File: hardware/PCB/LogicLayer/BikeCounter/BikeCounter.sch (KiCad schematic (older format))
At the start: 18 parts, among them J1 PIR sensor connector (TWIG-4P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, J2 Conn_01x04_Female, J3 Conn_01x02_Female, SW1 SW_DIP_x03, U1 DS3231M

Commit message: PCB layout splitted into power and logic layer
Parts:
- removed BT1: Battery_Cell, Battery:BatteryHolder_Keystone_1042_1x18650, symbol Device:Battery_Cell
- removed J3: Conn_01x02_Female, symbol Connector:Conn_01x02_Female
- added J3: Vbat, Connector_PinSocket_2.54mm:PinSocket_1x01_P2.54mm_Vertical, symbol Connector:Conn_01x01_Female
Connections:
- net labels removed: +3V8
- wire segments 72 -> 65
- no-connect marks 26 -> 27
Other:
- moved on the sheet: C1, J1, R1, R2
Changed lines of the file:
@@
-$EndComp
-$Comp
-L Device:Battery_Cell BT1
-U 1 1 615B5A8C
-P 3300 1950
-F 0 "BT1" H 3418 2046 50  0000 L CNN
-F 1 "Battery_Cell" H 3418 1955 50  0000 L CNN
-F 2 "Battery:BatteryHolder_Keystone_1042_1x18650" V 3300 2010 50  0001 C CNN
-F 3 "~" V 3300 2010 50  0001 C CNN
-	1    3300 1950
-	1    0    0    -1
-$EndComp
-$Comp
-L power:+3V8 #PWR0101
-U 1 1 615B6BD8
-P 3300 1750
-F 0 "#PWR0101" H 3300 1600 50  0001 C CNN
-F 1 "+3V8" H 3315 1923 50  0000 C CNN
-F 2 "" H 3300 1750 50  0001 C CNN
-F 3 "" H 3300 1750 50  0001 C CNN
-	1    3300 1750
-	1    0    0    -1
-$EndComp
-$Comp
-L power:+3V8 #PWR0102
-U 1 1 615B7800
-P 4350 2100
-F 0 "#PWR0102" H 4350 1950 50  0001 C CNN
-F 1 "+3V8" H 4365 2273 50  0000 C CNN
-F 2 "" H 4350 2100 50  0001 C CNN
-F 3 "" H 4350 2100 50  0001 C CNN
-	1    4350 2100
-	1    0    0    -1
-$EndComp
-$Comp
-L power:GND #PWR0103
-U 1 1 615B8DA8
-P 3300 2050
-F 0 "#PWR0103" H 3300 1800 50  0001 C CNN
-F 1 "GND" H 3305 1877 50  0000 C CNN
-F 2 "" H 3300 2050 50  0001 C CNN
-F 3 "" H 3300 2050 50  0001 C CNN
-	1    3300 2050
-	1    0    0    -1
 $EndComp
 $Comp
 L Device:R R2
 U 1 1 615B9C8E
-P 4050 2750
-F 0 "R2" H 4120 2796 50  0000 L CNN
-F 1 "1.2M" H 4120 2705 50  0000 L CNN
-F 2 "Resistor_SMD:R_1206_3216Metric_Pad1.42x1.75mm_HandSolder" V 3980 2750 50  0001 C CNN
-F 3 "~" H 4050 2750 50  0001 C CNN
-	1    4050 2750
+P 4050 3700
+F 0 "R2" H 4120 3746 50  0000 L CNN
+F 1 "1.2M" H 4120 3655 50  0000 L CNN
+F 2 "Resistor_SMD:R_1206_3216Metric_Pad1.42x1.75mm_HandSolder" V 3980 3700 50  0001 C CNN
+F 3 "~" H 4050 3700 50  0001 C CNN
+	1    4050 3700
 	1    0    0    -1
 $EndComp
@@
 L Device:R R1
 U 1 1 615BA347
-P 4050 2350
-F 0 "R1" H 4120 2396 50  0000 L CNN
-F 1 "330k" H 4120 2305 50  0000 L CNN
-F 2 "Resistor_SMD:R_1206_3216Metric_Pad1.42x1.75mm_HandSolder" V 3980 2350 50  0001 C CNN
-F 3 "~" H 4050 2350 50  0001 C CNN
-	1    4050 2350
+P 4050 3300
+F 0 "R1" H 4120 3346 50  0000 L CNN
+F 1 "330k" H 4120 3255 50  0000 L CNN
+F 2 "Resistor_SMD:R_1206_3216Metric_Pad1.42x1.75mm_HandSolder" V 3980 3300 50  0001 C CNN
+F 3 "~" H 4050 3300 50  0001 C CNN
+	1    4050 3300
 	1    0    0    -1
 $EndComp
@@
 L Device:C C1
 U 1 1 615B5D7E
-P 3600 2750
-F 0 "C1" H 3715 2796 50  0000 L CNN
-F 1 "0.1uF" H 3715 2705 50  0000 L CNN
-F 2 "Capacitor_SMD:C_0805_2012Metric_Pad1.15x1.40mm_HandSolder" H 3638 2600 50  0001 C CNN
-F 3 "~" H 3600 2750 50  0001 C CNN
-	1    3600 2750
-	1    0    0    -1
-$EndComp
-Wire Wire Line
-	4050 2500 4050 2550
-Wire Wire Line
-	3600 2600 3600 2550
-Wire Wire Line
-	3600 2550 4050 2550
-Connection ~ 4050 2550
-Wire Wire Line
-	4050 2550 4050 2600
-Wire Wire Line
-	4400 3000 4050 3000
-Wire Wire Line
-	4050 3000 4050 2900
-Wire Wire Line
-	4050 3000 3600 3000
-Wire Wire Line
-	3600 3000 3600 2900
-Connection ~ 4050 3000
+P 3600 3700
+F 0 "C1" H 3715 3746 50  0000 L CNN
+F 1 "0.1uF" H 3715 3655 50  0000 L CNN
+F 2 "Capacitor_SMD:C_0805_2012Metric_Pad1.15x1.40mm_HandSolder" H 3638 3550 50  0001 C CNN
+F 3 "~" H 3600 3700 50  0001 C CNN
+	1    3600 3700
+	1    0    0    -1
+$EndComp
+Wire Wire Line
+	4050 3450 4050 3500
+Wire Wire Line
+	3600 3550 3600 3500
+Wire Wire Line
+	3600 3500 4050 3500
+Connection ~ 4050 3500
+Wire Wire Line
+	4050 3500 4050 3550
+Wire Wire Line
+	4050 3950 4050 3850
+Wire Wire Line
+	4050 3950 3600 3950
+Wire Wire Line
+	3600 3950 3600 3850
 $Comp
 L power:GND #PWR0104
 U 1 1 615B913B
-P 3600 3050
-F 0 "#PWR0104" H 3600 2800 50  0001 C CNN
-F 1 "GND" H 3605 2877 50  0000 C CNN
-F 2 "" H 3600 3050 50  0001 C CNN
-F 3 "" H 3600 3050 50  0001 C CNN
-	1    3600 3050
-	1    0    0    -1
-$EndComp
-Wire Wire Line
-	3600 3050 3600 3000
-Connection ~ 3600 3000
-Wire Wire Line
-	3600 2550 3300 2550
-Wire Wire Line
-	3300 2550 3300 3500
-Wire Wire Line
-	3300 3500 4950 3500
-Connection ~ 3600 2550
-Wire Wire Line
-	4400 2900 4350 2900
-Wire Wire Line
-	4350 2900 4350 2150
-Wire Wire Line
-	4050 2200 4050 2150
-Wire Wire Line
-	4050 2150 4350 2150
-Connection ~ 4350 2150
-Wire Wire Line
-	4350 2150 4350 2100
+P 3600 4000
+F 0 "#PWR0104" H 3600 3750 50  0001 C CNN
+F 1 "GND" H 3605 3827 50  0000 C CNN
+F 2 "" H 3600 4000 50  0001 C CNN
+F 3 "" H 3600 4000 50  0001 C CNN
+	1    3600 4000
+	1    0    0    -1
+$EndComp
+Wire Wire Line
+	3600 4000 3600 3950
+Connection ~ 3600 3950
 $Comp
 L Timer_RTC:DS3231M U1
@@
 L Connector:Conn_01x04_Male J1
 U 1 1 615E6BA2
-P 3050 4400
-F 0 "J1" H 3158 4681 50  0000 C CNN
-F 1 "PIR sensor connector (TWIG-4P-2.0)" H 3158 4590 50  0000 C CNN
-F 2 "Connector_PinSocket_2.00mm:PinSocket_1x04_P2.00mm_Vertical" H 3050 4400 50  0001 C CNN
-F 3 "~" H 3050 4400 50  0001 C CNN
-	1    3050 4400
+P 3600 5050
+F 0 "J1" H 3708 5331 50  0000 C CNN
+F 1 "PIR sensor connector (TWIG-4P-2.0)" H 3708 5240 50  0000 C CNN
+F 2 "Connector_PinSocket_2.00mm:PinSocket_1x04_P2.00mm_Vertical" H 3600 5050 50  0001 C CNN
+F 3 "~" H 3600 5050 50  0001 C CNN
+	1    3600 5050
 	1    0    0    -1
 $EndComp
@@
 	6450 1550 6300 1550
 Wire Wire Line
-	3250 4300 3400 4300
+	3800 4950 3950 4950
 $Comp
 L power:+3.3V #PWR0116
 U 1 1 61601685
-P 3400 4500
-F 0 "#PWR0116" H 3400 4350 50  0001 C CNN
-F 1 "+3.3V" V 3415 4628 50  0000 L CNN
-F 2 "" H 3400 4500 50  0001 C CNN
-F 3 "" H 3400 4500 50  0001 C CNN
-	1    3400 4500
+P 3950 5150
+F 0 "#PWR0116" H 3950 5000 50  0001 C CNN
+F 1 "+3.3V" V 3965 5278 50  0000 L CNN
+F 2 "" H 3950 5150 50  0001 C CNN
+F 3 "" H 3950 5150 50  0001 C CNN
+	1    3950 5150
 	0    1    1    0
 $EndComp
@@
 L power:GND #PWR0117
 U 1 1 61602198
-P 3400 4600
-F 0 "#PWR0117" H 3400 4350 50  0001 C CNN
-F 1 "GND" H 3405 4427 50  0000 C CNN
-F 2 "" H 3400 4600 50  0001 C CNN
-F 3 "" H 3400 4600 50  0001 C CNN
-	1    3400 4600
-	1    0    0    -1
-$EndComp
-Wire Wire Line
-	3250 4500 3400 4500
-Wire Wire Line
-	3250 4600 3400 4600
-NoConn ~ 3250 4400
-Text GLabel 3400 4300 2    50   Input ~ 0
+P 3950 5250
+F 0 "#PWR0117" H 3950 5000 50  0001 C CNN
+F 1 "GND" H 3955 5077 50  0000 C CNN
+F 2 "" H 3950 5250 50  0001 C CNN
+F 3 "" H 3950 5250 50  0001 C CNN
+	1    3950 5250
+	1    0    0    -1
+$EndComp
+Wire Wire Line
+	3800 5150 3950 5150
+Wire Wire Line
+	3800 5250 3950 5250
+NoConn ~ 3800 5050
+Text GLabel 3950 4950 2    50   Input ~ 0
 PIR_signal
 Text GLabel 4800 4300 0    50   Input ~ 0
@@
 	1    0    0    -1
 $EndComp
-$Comp
-L Connector:Conn_01x02_Female J3
-U 1 1 616961B5
-P 4600 2900
-F 0 "J3" H 4628 2876 50  0000 L CNN
-F 1 "Conn_01x02_Female" H 4150 2700 50  0000 L CNN
-F 2 "" H 4600 2900 50  0001 C CNN
-F 3 "~" H 4600 2900 50  0001 C CNN
-	1    4600 2900
-	1    0    0    -1
-$EndComp
 NoConn ~ 4950 2900
 NoConn ~ 4950 3000
+NoConn ~ 5550 1050
+$Comp
+L Connector:Conn_01x01_Female J3
+U 1 1 61A49201
+P 3850 3000
+F 0 "J3" H 3742 3185 50  0000 C CNN
+F 1 "Vbat" H 3742 3094 50  0000 C CNN
+F 2 "Connector_PinSocket_2.54mm:PinSocket_1x01_P2.54mm_Vertical" H 3850 3000 50  0001 C CNN
+F 3 "~" H 3850 3000 50  0001 C CNN
+	1    3850 3000
+	-1   0    0    -1
+$EndComp
+Wire Wire Line
+	4050 3000 4050 3150
+Wire Wire Line
+	4050 3500 4950 3500
 $EndSCHEMATC

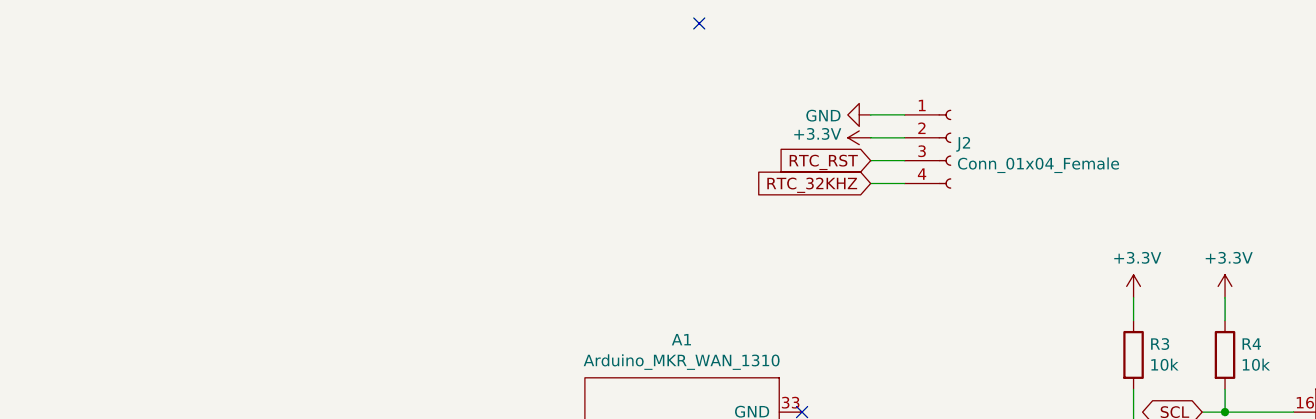
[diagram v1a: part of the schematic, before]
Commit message: Humidity sensor to pcb added
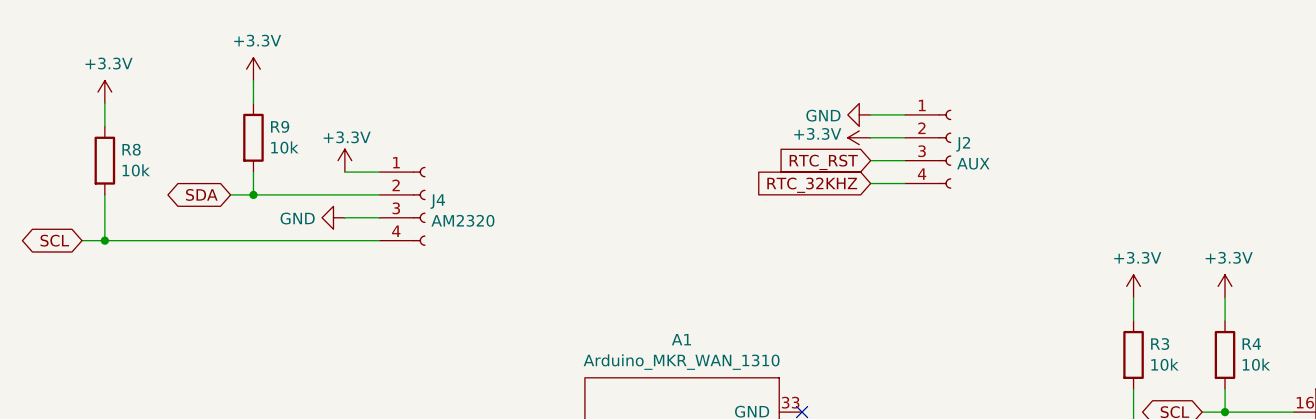
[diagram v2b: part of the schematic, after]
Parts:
- added J4: AM2320, Connector_PinSocket_2.54mm:PinSocket_1x04_P2.54mm_Vertical, symbol Connector:Conn_01x04_Female
- added R8, R9: 10k, Resistor_SMD:R_1206_3216Metric_Pad1.42x1.75mm_HandSolder, symbol Device:R
- J2: value Conn_01x04_Female -> AUX
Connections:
- net +3V3: now also J4.1 (Pin_1), R8.1, R9.1
- net GND: now also J4.3 (Pin_3)
- net SCL: now also J4.4 (Pin_4), R8.2
- net SDA: now also J4.2 (Pin_2), R9.2
- no-connect marks 27 -> 26
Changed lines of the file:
@@
 P 6650 1550
 F 0 "J2" H 6678 1526 50  0000 L CNN
-F 1 "Conn_01x04_Female" H 6678 1435 50  0000 L CNN
+F 1 "AUX" H 6678 1435 50  0000 L CNN
 F 2 "Connector_PinSocket_2.54mm:PinSocket_1x04_P2.54mm_Vertical" H 6650 1550 50  0001 C CNN
 F 3 "~" H 6650 1550 50  0001 C CNN
@@
 NoConn ~ 4950 2900
 NoConn ~ 4950 3000
-NoConn ~ 5550 1050
 $Comp
 L Connector:Conn_01x01_Female J3
@@
 Wire Wire Line
 	4050 3500 4950 3500
+$Comp
+L Connector:Conn_01x04_Female J4
+U 1 1 61AC02D4
+P 4350 1800
+F 0 "J4" H 4378 1776 50  0000 L CNN
+F 1 "AM2320" H 4378 1685 50  0000 L CNN
+F 2 "Connector_PinSocket_2.54mm:PinSocket_1x04_P2.54mm_Vertical" H 4350 1800 50  0001 C CNN
+F 3 "~" H 4350 1800 50  0001 C CNN
+	1    4350 1800
+	1    0    0    -1
+$EndComp
+Wire Wire Line
+	4000 1900 4150 1900
+$Comp
+L power:GND #PWR0101
+U 1 1 61AC02DC
+P 4000 1900
+F 0 "#PWR0101" H 4000 1650 50  0001 C CNN
+F 1 "GND" V 4005 1772 50  0000 R CNN
+F 2 "" H 4000 1900 50  0001 C CNN
+F 3 "" H 4000 1900 50  0001 C CNN
+	1    4000 1900
+	0    1    1    0
+$EndComp
+$Comp
+L power:+3.3V #PWR0102
+U 1 1 61AC02E2
+P 4000 1700
+F 0 "#PWR0102" H 4000 1550 50  0001 C CNN
+F 1 "+3.3V" H 3900 1850 50  0000 L CNN
+F 2 "" H 4000 1700 50  0001 C CNN
+F 3 "" H 4000 1700 50  0001 C CNN
+	1    4000 1700
+	1    0    0    -1
+$EndComp
+Wire Wire Line
+	4150 1700 4000 1700
+$Comp
+L Device:R R9
+U 1 1 61AC74CB
+P 3600 1550
+F 0 "R9" H 3670 1596 50  0000 L CNN
+F 1 "10k" H 3670 1505 50  0000 L CNN
+F 2 "Resistor_SMD:R_1206_3216Metric_Pad1.42x1.75mm_HandSolder" V 3530 1550 50  0001 C CNN
+F 3 "~" H 3600 1550 50  0001 C CNN
+	1    3600 1550
+	1    0    0    -1
+$EndComp
+$Comp
+L Device:R R8
+U 1 1 61AC74D1
+P 2950 1650
+F 0 "R8" H 3020 1696 50  0000 L CNN
+F 1 "10k" H 3020 1605 50  0000 L CNN
+F 2 "Resistor_SMD:R_1206_3216Metric_Pad1.42x1.75mm_HandSolder" V 2880 1650 50  0001 C CNN
+F 3 "~" H 2950 1650 50  0001 C CNN
+	1    2950 1650
+	1    0    0    -1
+$EndComp
+Wire Wire Line
+	3600 1800 3600 1700
+Text GLabel 3500 1800 0    50   BiDi ~ 0
+SDA
+Text GLabel 2850 2000 0    50   BiDi ~ 0
+SCL
+Wire Wire Line
+	2950 1800 2950 2000
+Wire Wire Line
+	2950 2000 4150 2000
+Wire Wire Line
+	2950 2000 2850 2000
+Connection ~ 2950 2000
+Wire Wire Line
+	3600 1800 3500 1800
+Connection ~ 3600 1800
+$Comp
+L power:+3.3V #PWR04
+U 1 1 61AC74E1
+P 2950 1400
+F 0 "#PWR04" H 2950 1250 50  0001 C CNN
+F 1 "+3.3V" H 2965 1573 50  0000 C CNN
+F 2 "" H 2950 1400 50  0001 C CNN
+F 3 "" H 2950 1400 50  0001 C CNN
+	1    2950 1400
+	1    0    0    -1
+$EndComp
+$Comp
+L power:+3.3V #PWR05
+U 1 1 61AC74E7
+P 3600 1300
+F 0 "#PWR05" H 3600 1150 50  0001 C CNN
+F 1 "+3.3V" H 3615 1473 50  0000 C CNN
+F 2 "" H 3600 1300 50  0001 C CNN
+F 3 "" H 3600 1300 50  0001 C CNN
+	1    3600 1300
+	1    0    0    -1
+$EndComp
+Wire Wire Line
+	2950 1400 2950 1500
+Wire Wire Line
+	3600 1300 3600 1400
+Wire Wire Line
+	3600 1800 4150 1800
 $EndSCHEMATC
